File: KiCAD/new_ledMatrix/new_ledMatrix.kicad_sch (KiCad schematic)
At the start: 61 parts

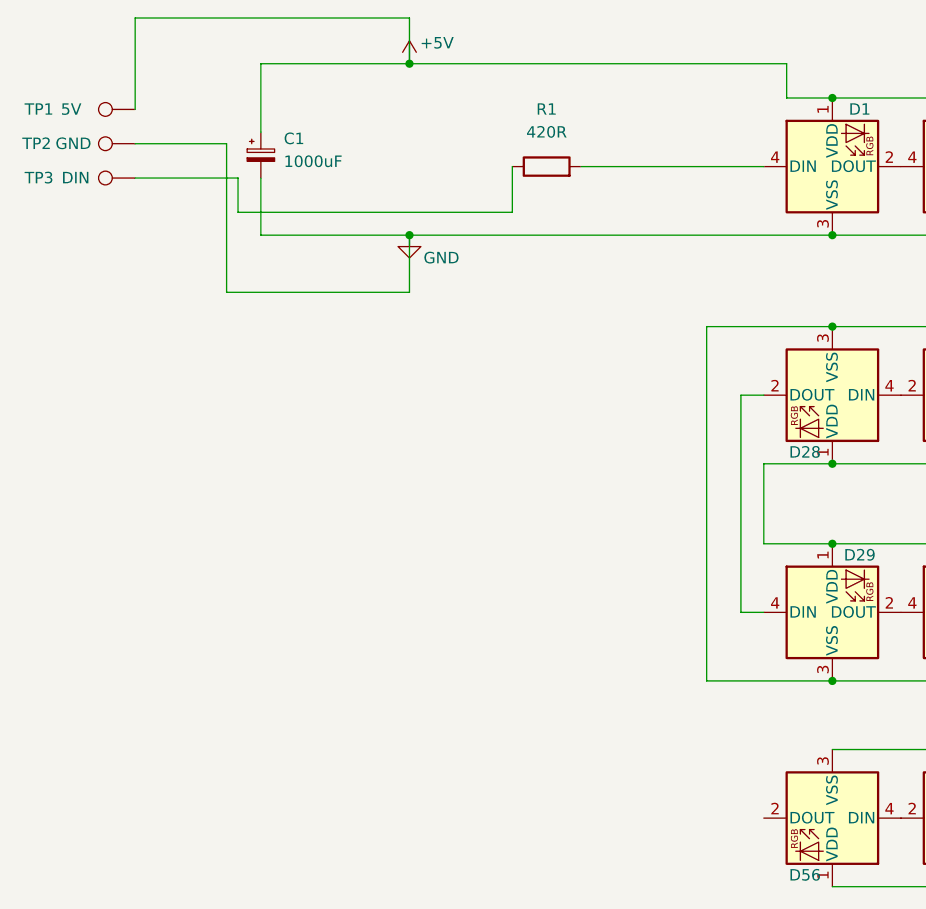
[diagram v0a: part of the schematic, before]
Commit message: added DOUT in PCB
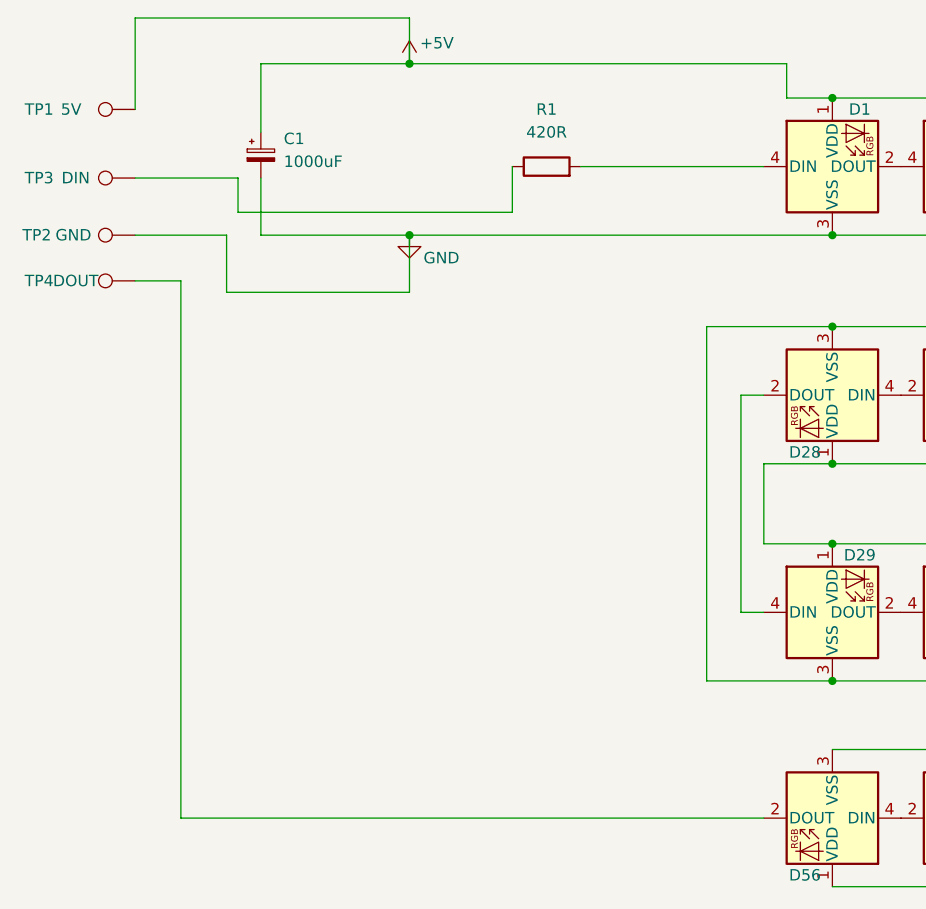
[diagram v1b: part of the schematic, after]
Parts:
- added TP4: DOUT, TestPoint:TestPoint_Pad_D2.5mm, symbol Connector:TestPoint
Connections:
- net at D56.2 (DOUT): now also TP4.1
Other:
- moved on the sheet: TP2
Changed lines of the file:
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@@
 	(wire
 		(pts
+			(xy 73.66 71.12) (xy 73.66 130.81)
+		)
+		(stroke
+			(width 0)
+			(type default)
+		)
+	)
+	(wire
+		(pts
 			(xy 252.73 66.04) (xy 267.97 66.04)
 		)
@@
 	(wire
 		(pts
+			(xy 73.66 71.12) (xy 68.58 71.12)
+		)
+		(stroke
+			(width 0)
+			(type default)
+		)
+	)
+	(wire
+		(pts
 			(xy 298.45 66.04) (xy 313.69 66.04)
 		)
@@
 	(wire
 		(pts
-			(xy 68.58 55.88) (xy 78.74 55.88)
+			(xy 68.58 66.04) (xy 78.74 66.04)
 		)
 		(stroke
@@
 	(wire
 		(pts
+			(xy 138.43 130.81) (xy 73.66 130.81)
+		)
+		(stroke
+			(width 0)
+			(type default)
+		)
+	)
+	(wire
+		(pts
 			(xy 328.93 138.43) (xy 344.17 138.43)
 		)
@@
 	(wire
 		(pts
-			(xy 78.74 55.88) (xy 78.74 72.39)
+			(xy 78.74 66.04) (xy 78.74 72.39)
 		)
 		(stroke
@@
 	)
 	(symbol
+		(lib_id "Connector:TestPoint")
+		(at 68.58 71.12 90)
+		(unit 1)
+		(exclude_from_sim no)
+		(in_bom yes)
+		(on_board yes)
+		(dnp no)
+		(property "Reference" "TP4"
+			(at 57.912 71.12 90)
+			(effects
+				(font
+					(size 1.27 1.27)
+				)
+			)
+		)
+		(property "Value" "DOUT"
+			(at 61.976 71.12 90)
+			(effects
+				(font
+					(size 1.27 1.27)
+				)
+			)
+		)
+		(property "Footprint" "TestPoint:TestPoint_Pad_D2.5mm"
+			(at 68.58 66.04 0)
+			(effects
+				(font
+					(size 1.27 1.27)
+				)
+				(hide yes)
+			)
+		)
+		(property "Datasheet" "~"
+			(at 68.58 66.04 0)
+			(effects
+				(font
+					(size 1.27 1.27)
+				)
+				(hide yes)
+			)
+		)
+		(property "Description" "test point"
+			(at 68.58 71.12 0)
+			(effects
+				(font
+					(size 1.27 1.27)
+				)
+				(hide yes)
+			)
+		)
+		(pin "1"
+		)
+		(instances
+			(project "new_ledMatrix"
+				(path "/7ce00b61-7069-44ef-8095-8ca0ad9d42b3"
+					(reference "TP4")
+					(unit 1)
+				)
+			)
+		)
+	)
+	(symbol
 		(lib_id "My_Custom_Symbols:WS2812B-Mini")
 		(at 267.97 58.42 90)
@@
 	(symbol
 		(lib_id "Connector:TestPoint")
-		(at 68.58 55.88 90)
+		(at 68.58 66.04 90)
 		(unit 1)
 		(exclude_from_sim no)
@@
 		(dnp no)
 		(property "Reference" "TP2"
-			(at 57.658 55.88 90)
+			(at 57.658 66.04 90)
 			(effects
 				(font
@@
 		)
 		(property "Value" "GND"
-			(at 61.722 55.88 90)
+			(at 61.722 66.04 90)
 			(effects
 				(font
@@
 		)
 		(property "Footprint" "TestPoint:TestPoint_Pad_D2.5mm"
-			(at 68.58 50.8 0)
+			(at 68.58 60.96 0)
 			(effects
 				(font
@@
 		)
 		(property "Datasheet" "~"
-			(at 68.58 50.8 0)
+			(at 68.58 60.96 0)
 			(effects
 				(font
@@
 		)
 		(property "Description" "test point"
-			(at 68.58 55.88 0)
+			(at 68.58 66.04 0)
 			(effects
 				(font
